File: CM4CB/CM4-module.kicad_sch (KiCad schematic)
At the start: 13 parts, among them J10 690-019-298-412, J15 Conn_01x22_Female, J16 Conn_01x22_Female, J22 690-019-298-412, J4 Conn_01x22_Female, J5 Conn_01x22_Female, J6 THD-02-R, U12 RT9742SNGV

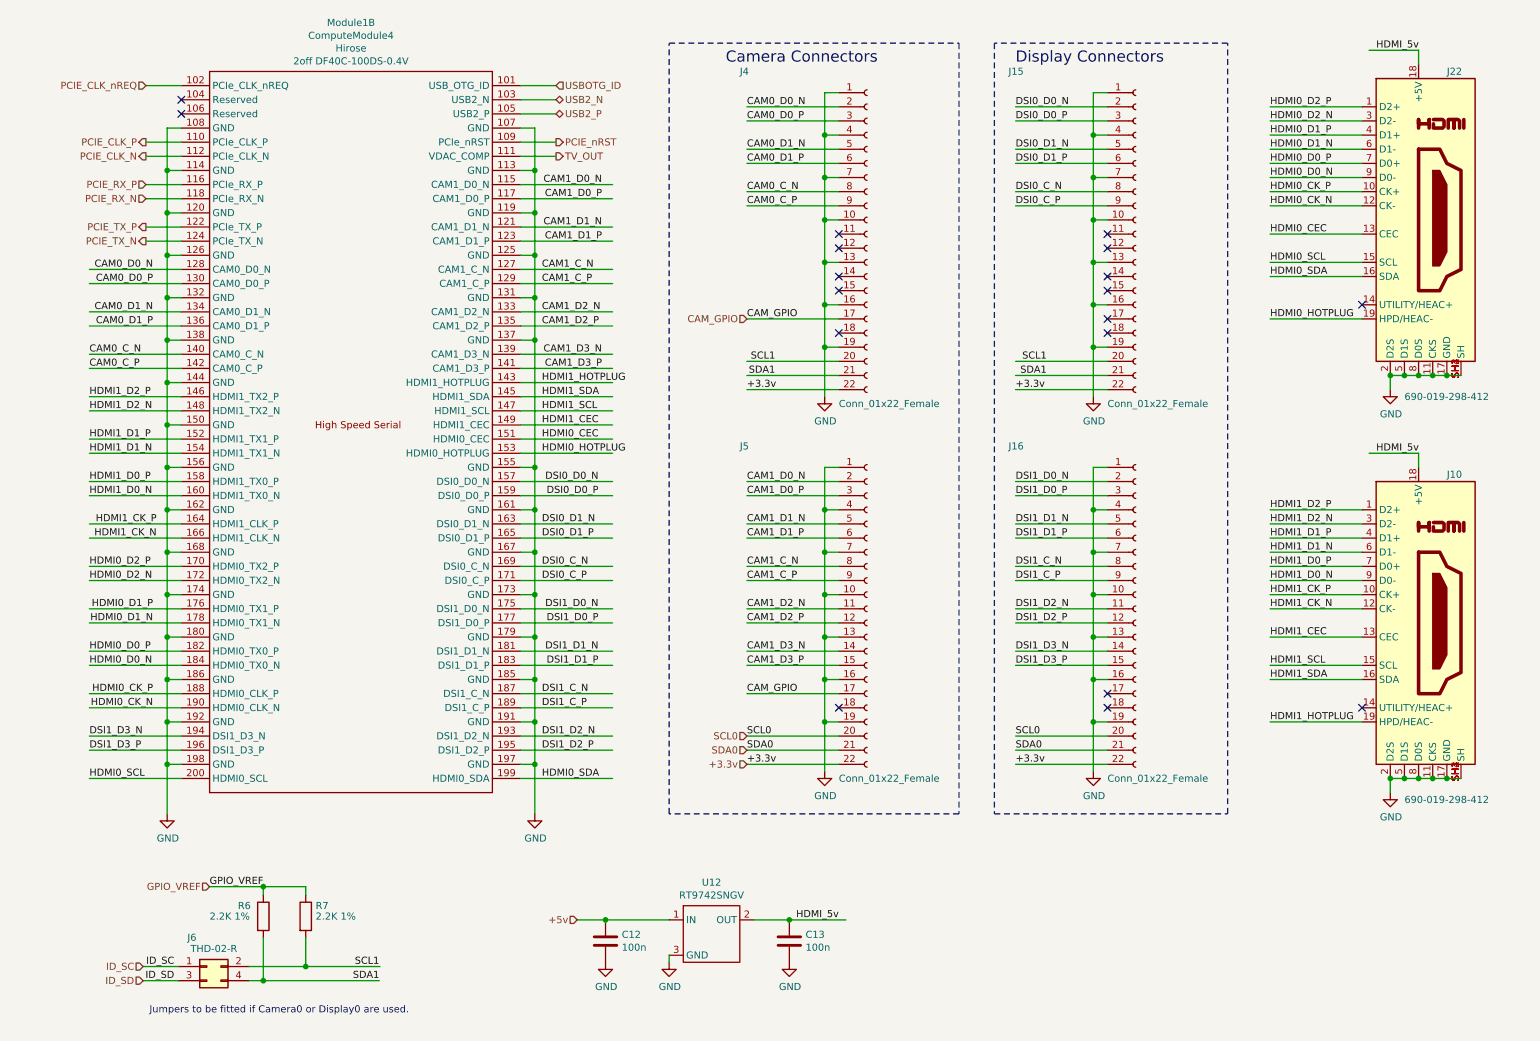
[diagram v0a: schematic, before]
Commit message: updated schematics
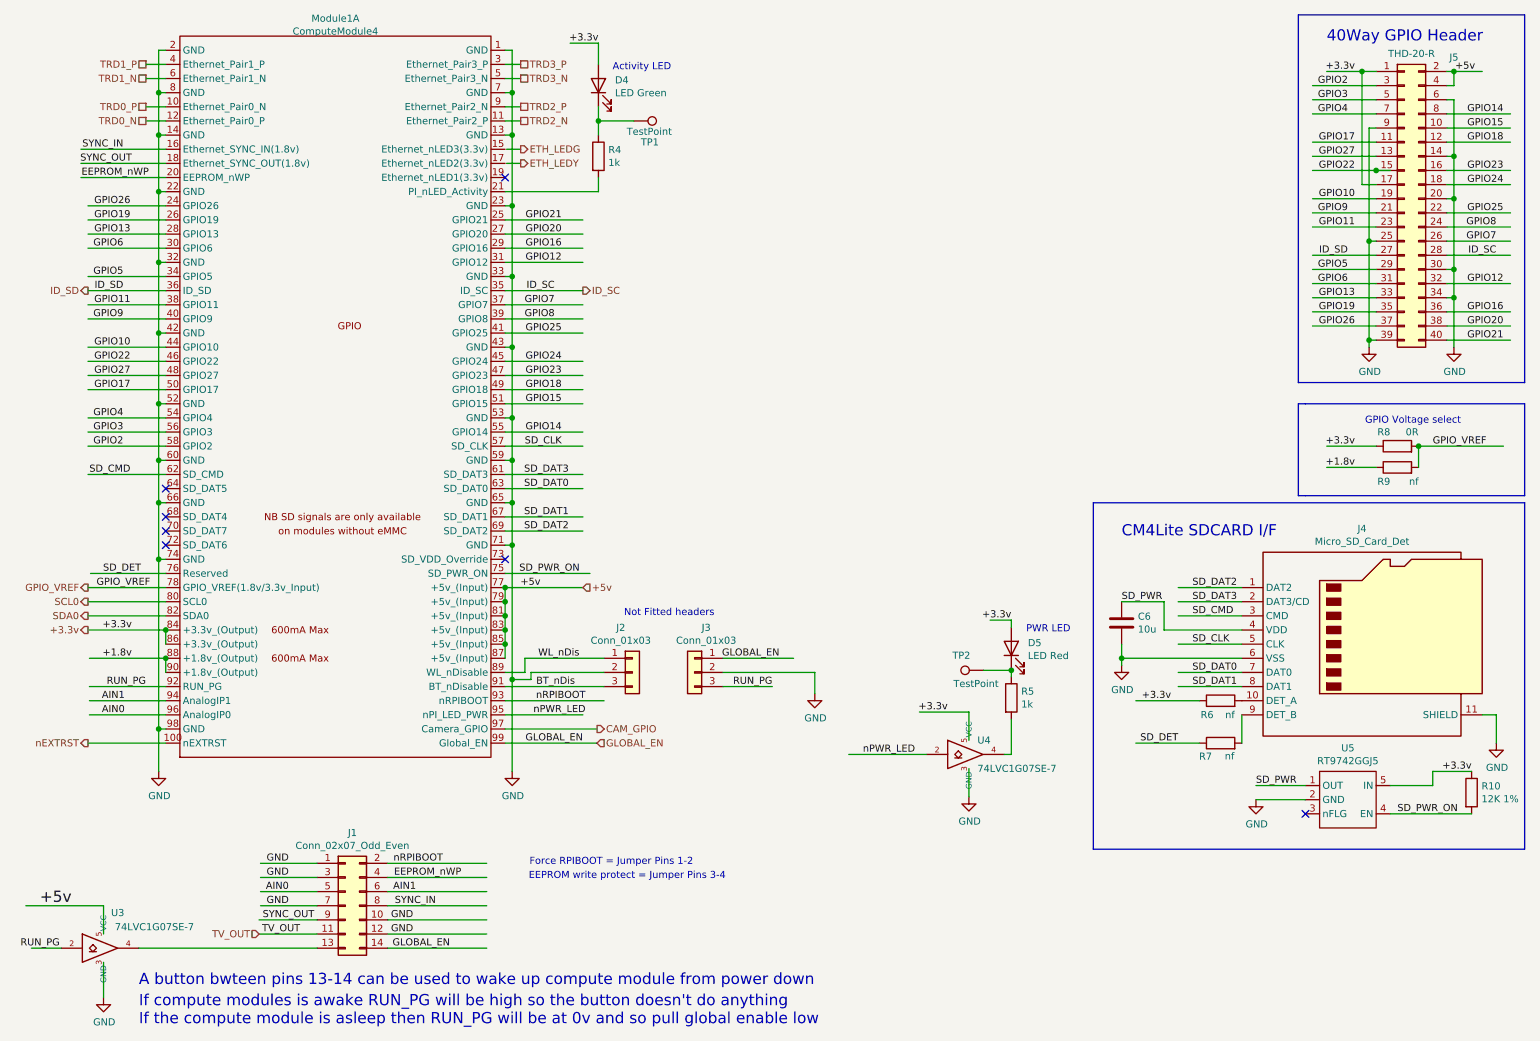
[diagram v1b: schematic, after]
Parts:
- removed C12, C13: 100n, Capacitor_SMD:C_0402_1005Metric, symbol Device:C
- removed J10, J22: 690-019-298-412, CM4IO:EDAC 690-019-298-412, symbol CM4IO:HDMI_A_1.4
- removed J15, J16, J4, J5: Conn_01x22_Female, Connector_FFC-FPC:Hirose_FH12-22S-0.5SH_1x22-1MP_P0.50mm_Horizontal, symbol Connector:Conn_01x22_Female
- removed J6: THD-02-R, Connector_PinHeader_2.54mm:PinHeader_2x02_P2.54mm_Vertical, symbol Connector_Generic:Conn_02x02_Odd_Even
- removed Module1: ComputeModule4, CM4IO:Raspberry-Pi-4-Compute-Module, symbol CM4IO:ComputeModule4-CM4
- removed U12: RT9742SNGV, Package_TO_SOT_SMD:SOT-23, symbol CM4IO:RT9742SNGV
- added C6: 10u, Capacitor_SMD:C_0805_2012Metric, symbol Device:C
- added D4: LED Green, LED_SMD:LED_0603_1608Metric, symbol Device:LED
- added D5: LED Red, LED_SMD:LED_0603_1608Metric, symbol Device:LED
- added J1: Conn_02x07_Odd_Even, Connector_PinHeader_2.54mm:PinHeader_2x07_P2.54mm_Vertical, symbol Connector_Generic:Conn_02x07_Odd_Even
- added J2, J3: Conn_01x03, Connector_PinHeader_2.54mm:PinHeader_1x03_P2.54mm_Vertical, symbol Connector_Generic:Conn_01x03
- added J4: Micro_SD_Card_Det, CM4IO:SDCARD_MOLEX_503398-1892, symbol Connector:Micro_SD_Card_Det
- added J5: THD-20-R, Connector_PinHeader_2.54mm:PinHeader_2x20_P2.54mm_Vertical, symbol Connector_Generic:Conn_02x20_Odd_Even
- added Module1: ComputeModule4, CM4IO:Raspberry-Pi-4-Compute-Module, symbol CM4IO:ComputeModule4-CM4
- added R10: 12K 1%, Resistor_SMD:R_0402_1005Metric, symbol Device:R
- added R4, R5: 1k, Resistor_SMD:R_0402_1005Metric, symbol Device:R
- added R8: 0R, Resistor_SMD:R_0805_2012Metric_Pad1.15x1.40mm_HandSolder, symbol Device:R
- added R9: nf, Resistor_SMD:R_0805_2012Metric_Pad1.15x1.40mm_HandSolder, symbol Device:R
- added TP1, TP2: TestPoint, TestPoint:TestPoint_Pad_2.0x2.0mm, symbol Connector:TestPoint
- added U3, U4: 74LVC1G07SE-7, Package_TO_SOT_SMD:SOT-353_SC-70-5, symbol CM4IO:74LVC1G07_copy
- added U5: RT9742GGJ5, Package_TO_SOT_SMD:SOT-23-5, symbol CM4IO:RT9742GGJ5
- R6, R7: value 2.2K 1% -> nf; Field5 9239278 -> 9239235; Field6 RK73G1ETQTP2201D -> RK73H1ETTP1001F; Field8 120889581 -> 125049511; Part Description Resistor 2.2K M1005 1% 63mW -> Resistor 1K M1005 1% 63mW
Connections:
- net +3.3v: now also R6.1, D4.2 (A), D5.2 (A), J5.1 (Pin_1), J5.17 (Pin_17), Module1.84 (+3.3v_(Output)), Module1.86 (+3.3v_(Output)), R10.1, R8.1, U4.5 (VCC), U5.5 (IN)
- net +5v: now also J5.2 (Pin_2), J5.4 (Pin_4), Module1.77 (+5v_(Input)), Module1.79 (+5v_(Input)), Module1.81 (+5v_(Input)), Module1.83 (+5v_(Input)), Module1.85 (+5v_(Input)), Module1.87 (+5v_(Input)), U3.5 (VCC)
- net CAM_GPIO: now also Module1.97 (Camera_GPIO)
- net GND: now also C6.2, J1.1 (Pin_1), J1.10 (Pin_10), J1.12 (Pin_12), J1.3 (Pin_3), J1.7 (Pin_7), J2.2 (Pin_2), J3.2 (Pin_2), J4.11 (SHIELD), J4.6 (VSS), J5.14 (Pin_14), J5.20 (Pin_20), J5.25 (Pin_25), J5.30 (Pin_30), J5.34 (Pin_34), J5.39 (Pin_39), J5.6 (Pin_6), J5.9 (Pin_9), Module1.1 (GND), Module1.13 (GND), Module1.14 (GND), Module1.2 (GND), Module1.22 (GND), Module1.23 (GND), Module1.32 (GND), Module1.33 (GND), Module1.42 (GND), Module1.43 (GND), Module1.52 (GND), Module1.53 (GND), Module1.59 (GND), Module1.60 (GND), Module1.65 (GND), Module1.66 (GND), Module1.7 (GND), Module1.71 (GND), Module1.74 (GND), Module1.8 (GND), Module1.98 (GND), U3.3 (GND), U4.3 (GND), U5.2 (GND)
- net GPIO_VREF: now also Module1.78 (GPIO_VREF(1.8v/3.3v_Input)), R8.2, R9.2; no longer R6.1, R7.1
- net ID_SC: now also J5.28 (Pin_28), Module1.35 (ID_SC)
- net ID_SD: now also J5.27 (Pin_27), Module1.36 (ID_SD)
- net SCL0: now also Module1.80 (SCL0)
- net SDA0: now also Module1.82 (SDA0)
- net TV_OUT: now also J1.11 (Pin_11)
- net SCL1: no longer names the net of R7.2
- net SCL1: now also J4.9 (DET_B)
- net SDA1: no longer names the net of R6.2
- net SDA1: now also J4.10 (DET_A)
- new net: J1.13 (Pin_13), U3.4
- new net: D5.1 (K), R5.1, TP2.1
- new net: Module1.21 (PI_nLED_Activity), R4.2
- new net: R5.2, U4.4
- new net: D4.1 (K), R4.1, TP1.1
- new net +1.8v: Module1.88 (+1.8v_(Output)), Module1.90 (+1.8v_(Output)), R9.1
- new net AIN0: J1.5 (Pin_5), Module1.96 (AnalogIP0)
- new net AIN1: J1.6 (Pin_6), Module1.94 (AnalogIP1)
- new net BT_nDis: J2.3 (Pin_3), Module1.91 (BT_nDisable)
- new net EEPROM_nWP: J1.4 (Pin_4), Module1.20 (EEPROM_nWP)
- new net GLOBAL_EN: J1.14 (Pin_14), J3.1 (Pin_1), Module1.99 (Global_EN)
- new net GPIO10: J5.19 (Pin_19), Module1.44 (GPIO10)
- new net GPIO11: J5.23 (Pin_23), Module1.38 (GPIO11)
- new net GPIO12: J5.32 (Pin_32), Module1.31 (GPIO12)
- new net GPIO13: J5.33 (Pin_33), Module1.28 (GPIO13)
- new net GPIO14: J5.8 (Pin_8), Module1.55 (GPIO14)
- new net GPIO15: J5.10 (Pin_10), Module1.51 (GPIO15)
- new net GPIO16: J5.36 (Pin_36), Module1.29 (GPIO16)
- new net GPIO17: J5.11 (Pin_11), Module1.50 (GPIO17)
- new net GPIO18: J5.12 (Pin_12), Module1.49 (GPIO18)
- new net GPIO19: J5.35 (Pin_35), Module1.26 (GPIO19)
- new net GPIO2: J5.3 (Pin_3), Module1.58 (GPIO2)
- new net GPIO20: J5.38 (Pin_38), Module1.27 (GPIO20)
- new net GPIO21: J5.40 (Pin_40), Module1.25 (GPIO21)
- new net GPIO22: J5.15 (Pin_15), Module1.46 (GPIO22)
- new net GPIO23: J5.16 (Pin_16), Module1.47 (GPIO23)
- new net GPIO24: J5.18 (Pin_18), Module1.45 (GPIO24)
- new net GPIO25: J5.22 (Pin_22), Module1.41 (GPIO25)
- new net GPIO26: J5.37 (Pin_37), Module1.24 (GPIO26)
- new net GPIO27: J5.13 (Pin_13), Module1.48 (GPIO27)
- new net GPIO3: J5.5 (Pin_5), Module1.56 (GPIO3)
- new net GPIO4: J5.7 (Pin_7), Module1.54 (GPIO4)
- new net GPIO5: J5.29 (Pin_29), Module1.34 (GPIO5)
- new net GPIO6: J5.31 (Pin_31), Module1.30 (GPIO6)
- new net GPIO7: J5.26 (Pin_26), Module1.37 (GPIO7)
- new net GPIO8: J5.24 (Pin_24), Module1.39 (GPIO8)
- new net GPIO9: J5.21 (Pin_21), Module1.40 (GPIO9)
- new net RUN_PG: J3.3 (Pin_3), Module1.92 (RUN_PG), U3.2
- new net SD_CLK: J4.5 (CLK), Module1.57 (SD_CLK)
- new net SD_CMD: J4.3 (CMD), Module1.62 (SD_CMD)
- new net SD_DAT0: J4.7 (DAT0), Module1.63 (SD_DAT0)
- new net SD_DAT1: J4.8 (DAT1), Module1.67 (SD_DAT1)
- new net SD_DAT2: J4.1 (DAT2), Module1.69 (SD_DAT2)
- new net SD_DAT3: J4.2 (DAT3/CD), Module1.61 (SD_DAT3)
- new net SD_DET: Module1.76 (Reserved), R7.1
- new net SD_PWR: C6.1, J4.4 (VDD), U5.1 (OUT)
- new net SD_PWR_ON: Module1.75 (SD_PWR_ON), R10.2, U5.4 (EN)
- new net SYNC_IN: J1.8 (Pin_8), Module1.16 (Ethernet_SYNC_IN(1.8v))
- new net SYNC_OUT: J1.9 (Pin_9), Module1.18 (Ethernet_SYNC_OUT(1.8v))
- new net TRD0_N: Module1.12 (Ethernet_Pair0_P)
- new net TRD0_P: Module1.10 (Ethernet_Pair0_N)
- new net TRD1_N: Module1.6 (Ethernet_Pair1_N)
- new net TRD1_P: Module1.4 (Ethernet_Pair1_P)
- new net TRD2_N: Module1.11 (Ethernet_Pair2_P)
- new net TRD2_P: Module1.9 (Ethernet_Pair2_N)
- new net TRD3_N: Module1.5 (Ethernet_Pair3_N)
- new net TRD3_P: Module1.3 (Ethernet_Pair3_P)
- new net WL_nDis: J2.1 (Pin_1), Module1.89 (WL_nDisable)
- new net nEXTRST: Module1.100 (nEXTRST)
- new net nPWR_LED: Module1.95 (nPI_LED_PWR), U4.2
- new net nRPIBOOT: J1.2 (Pin_2), Module1.93 (nRPIBOOT)
- no-connect marks 18 -> 7
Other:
- note added: "40Way GPIO Header"
- note added: "A button bwteen pins 13-14 can be used to wake up compute module from power down"
- note added: "Activity LED"
- note added: "CM4Lite SDCARD I/F"
- note added: "EEPROM write protect = Jumper Pins 3-4"
- note added: "Force RPIBOOT = Jumper Pins 1-2"
- note added: "GPIO Voltage select"
- note added: "If compute modules is awake RUN_PG will be high so the button doesn't do anything If the compute module is asleep then RUN_PG will be at 0v and so pull global enable low"
- note added: "Not Fitted headers"
- note added: "PWR LED"
- note removed: "Camera Connectors"
- note removed: "Display Connectors"
- note removed: "Jumpers to be fitted if Camera0 or Display0 are used."
- company: (c) Raspberry Pi Trading 2020 -> (none)
- title: Compute Module 4 IO Board - CM4 - Highspeed -> (none)
